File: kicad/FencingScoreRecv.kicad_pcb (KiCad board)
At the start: 2 copper layers, 134 x 41 mm, 33 parts, among them IC1 PIC16F18323-I/JQ, U1 MCP1824S33/DB, U2 ULN2003AD

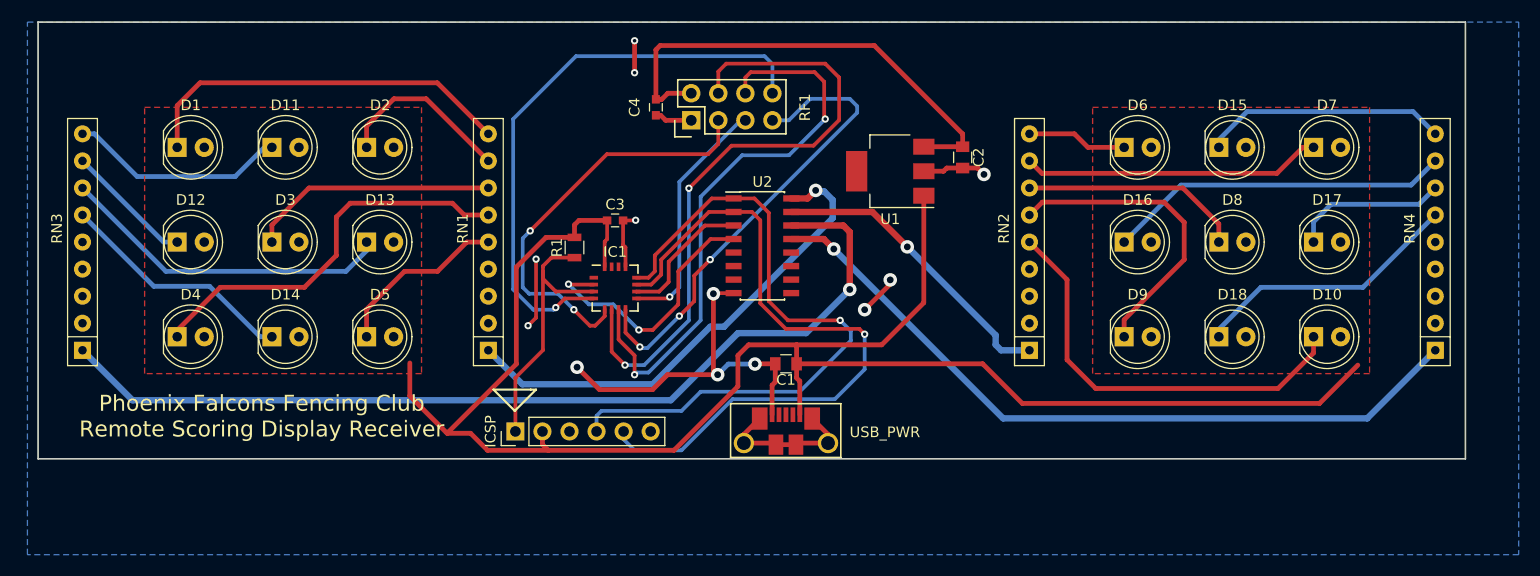
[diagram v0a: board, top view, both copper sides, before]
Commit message: Update RF addr and silkscreen, update for KiCad 7
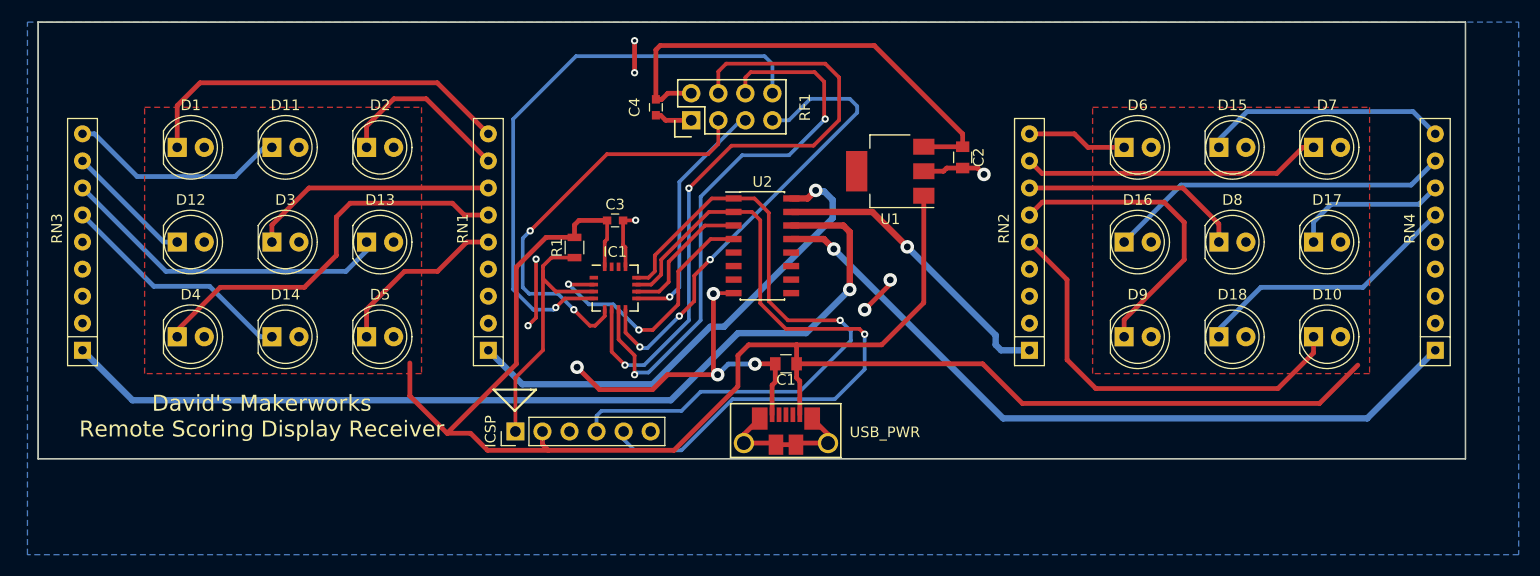
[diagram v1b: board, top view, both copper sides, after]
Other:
- net class Default removed
- board text added: "David's Makerworks Remote Scoring Display Receiver"
- board text removed: "Phoenix Falcons Fencing Club Remote Scoring Display Receiver"
